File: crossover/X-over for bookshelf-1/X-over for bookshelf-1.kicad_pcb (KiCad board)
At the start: 2 copper layers, 10 parts, among them J1 Screw_Terminal_01x02, J2 Screw_Terminal_01x04

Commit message: adding KiCAD documents for the XO design
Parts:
- moved C2 96.0 mm to (134.1, 132.1), turned to 180 degrees
- moved J2 64.5 mm to (193.0, 113.3), turned to 90 degrees
- moved L1 33.1 mm to (185.4, 49.0)
- moved J1 16.5 mm to (182.4, 38.1)
- moved C3 13.7 mm to (120.3, 68.6)
- moved C1 10.5 mm to (120.3, 45.7)
- moved R1 10.2 mm to (134.6, 104.1)
- moved R2 10.2 mm to (73.7, 86.4)
- moved L3 9.16 mm to (179.2, 106.7)
- moved L2 5.68 mm to (80.9, 55.9)
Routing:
- net Net-(J2-Pin_4): track 140.7 -> 31.9 mm
- net Net-(C2-Pad2): track 50.2 -> 115.6 mm
- net Net-(J2-Pin_2): track 156.3 -> 185.5 mm
- net Net-(J2-Pin_1): track 122.7 -> 146.5 mm
- net Net-(J1-Pin_2): track 157.1 -> 139.0 mm
- net Net-(J1-Pin_1): track 46.5 -> 32.1 mm
- net Net-(C3-Pad1): track 37.8 -> 23.7 mm
- net Net-(L3-Pad2): track 16.4 -> 12.4 mm
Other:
- board outline added: 139.7 x 119.4 mm

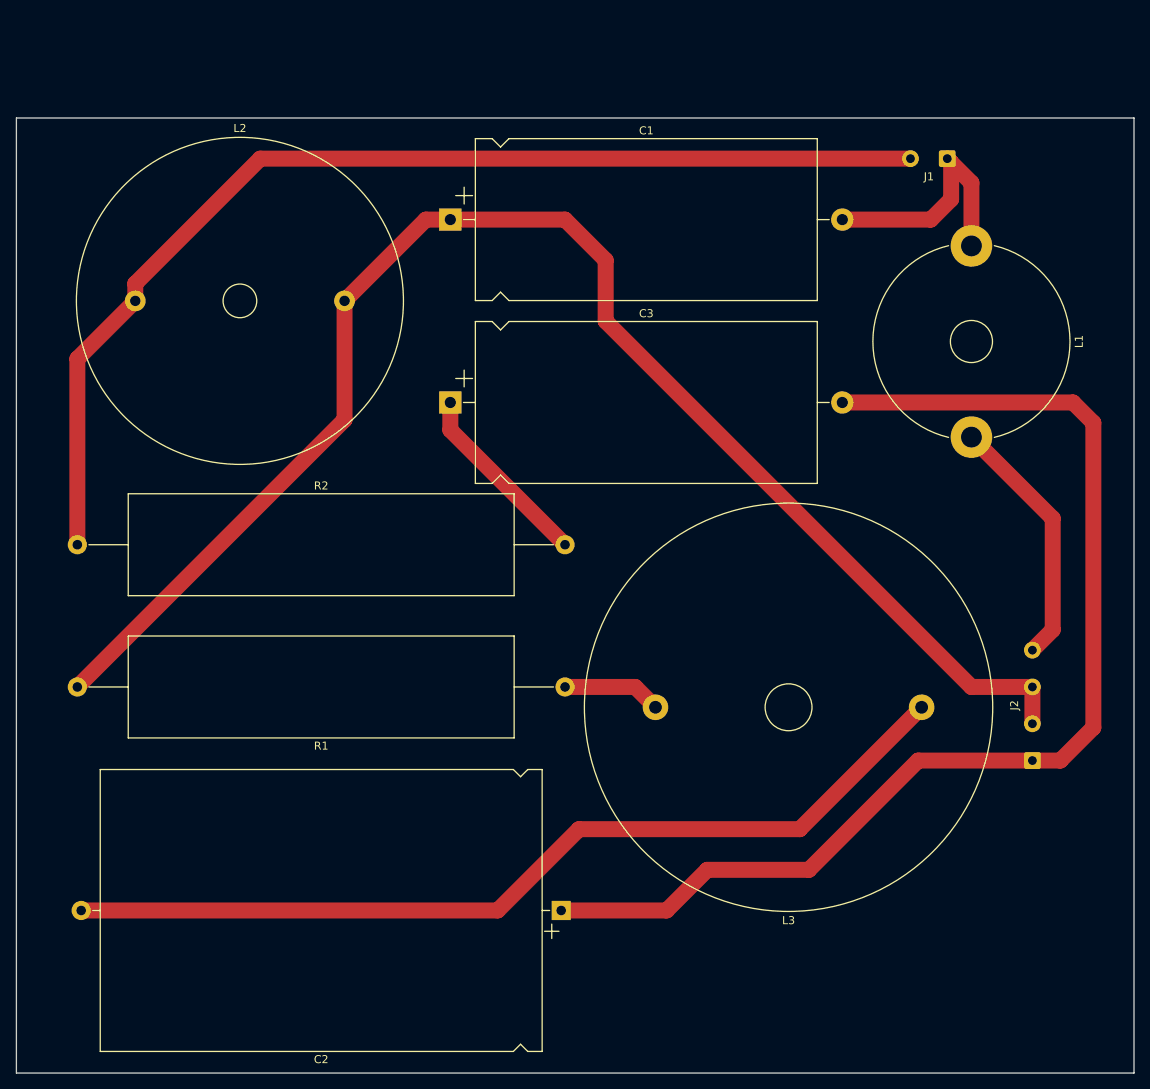
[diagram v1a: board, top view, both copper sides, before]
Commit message: Feature/pcb updates (#3)
* adding intial work to support PCB draw

* Minimizing overall PCB size

Now it should both fit inside the cabinet as well as through the driver opening.
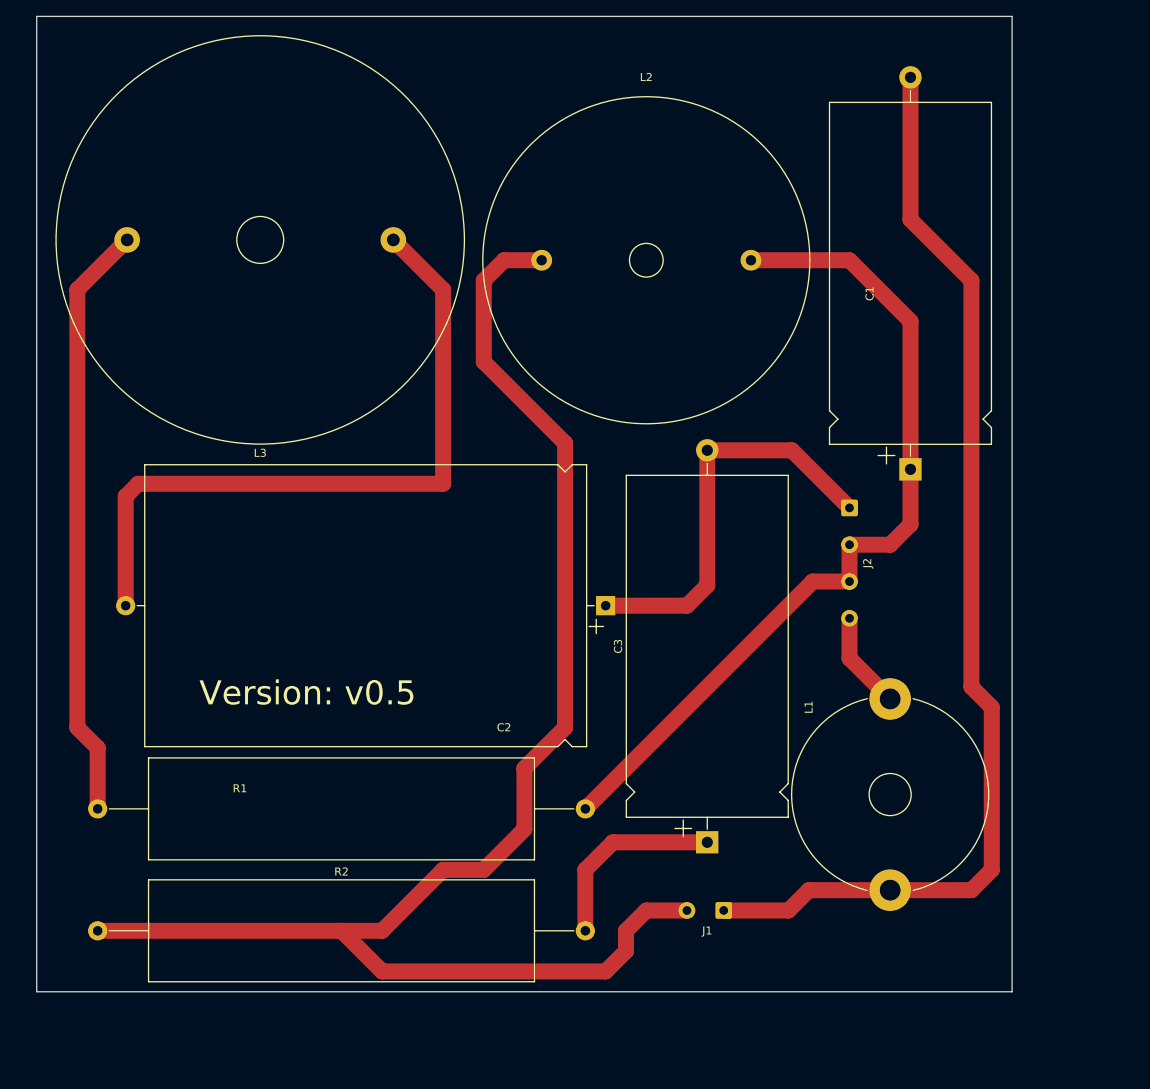
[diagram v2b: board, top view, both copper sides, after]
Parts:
- moved J1 98.0 mm to (154.5, 132.1)
- moved L3 88.2 mm to (113.2, 48.3)
- moved L1 81.2 mm to (175.3, 129.5), turned to 90 degrees
- moved C1 65.4 mm to (177.8, 76.9), turned to 90 degrees
- moved C3 63.7 mm to (152.4, 123.6), turned to 90 degrees
- moved R1 60.4 mm to (76.2, 119.4), turned to 0 degrees
- moved L2 51.1 mm to (131.7, 50.8)
- moved R2 48.3 mm to (76.2, 134.6)
- moved J2 39.0 mm to (170.2, 81.8), turned to -90 degrees
- moved C2 38.5 mm to (139.7, 94.0)
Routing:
- net Net-(J1-Pin_1): track 32.1 -> 138.9 mm
- net Net-(J2-Pin_1): track 146.5 -> 51.4 mm
- net Net-(J2-Pin_2): track 185.5 -> 106.6 mm
- net Net-(L3-Pad2): track 12.4 -> 74.8 mm
- net Net-(J1-Pin_2): track 139.0 -> 191.7 mm
- net Net-(C2-Pad2): track 115.6 -> 87.1 mm
- net Net-(J2-Pin_4): track 31.9 -> 12.2 mm
- net Net-(C3-Pad1): track 23.7 -> 24.3 mm
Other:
- board size 139.7 x 119.4 mm -> 121.9 x 121.9 mm
- board text added: "Version: v0.5"

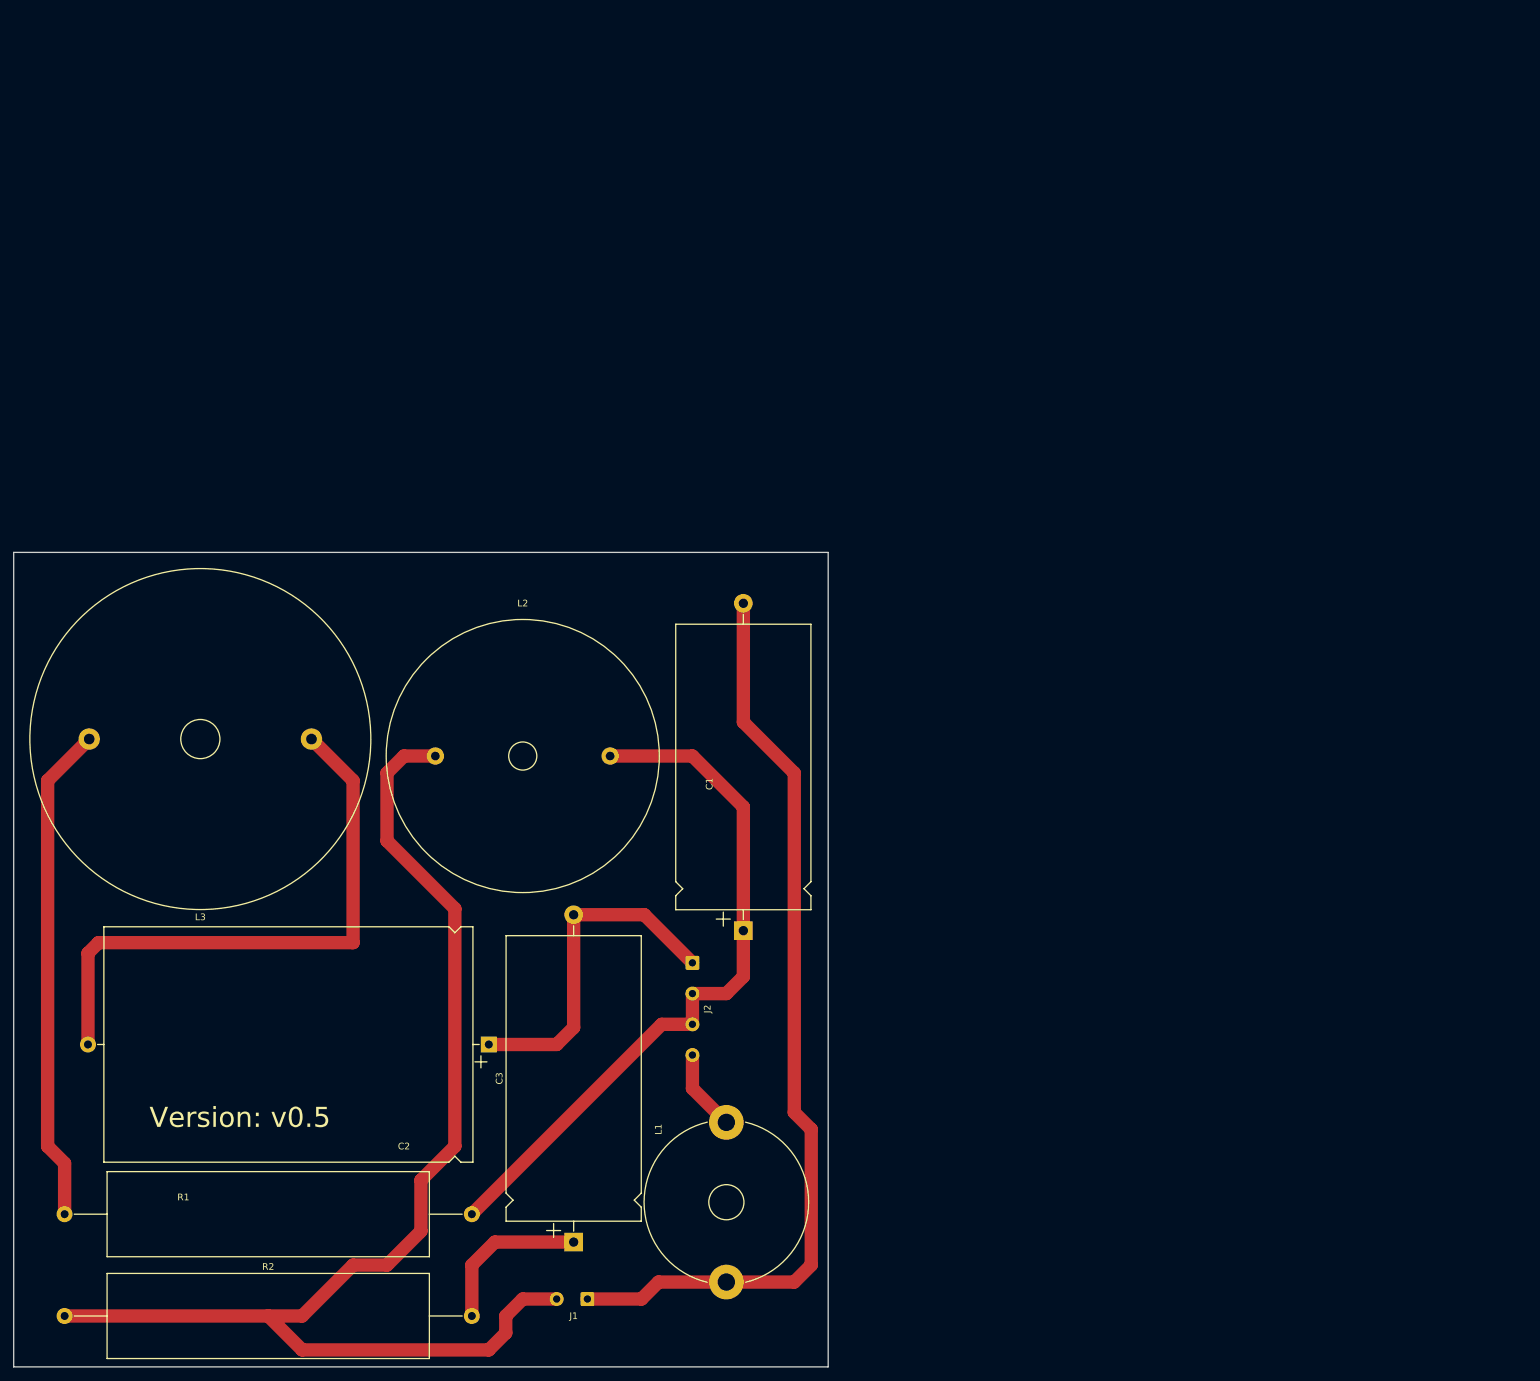
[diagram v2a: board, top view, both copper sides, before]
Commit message: Updated schematic and board layout, according to PdB Spec (#4)
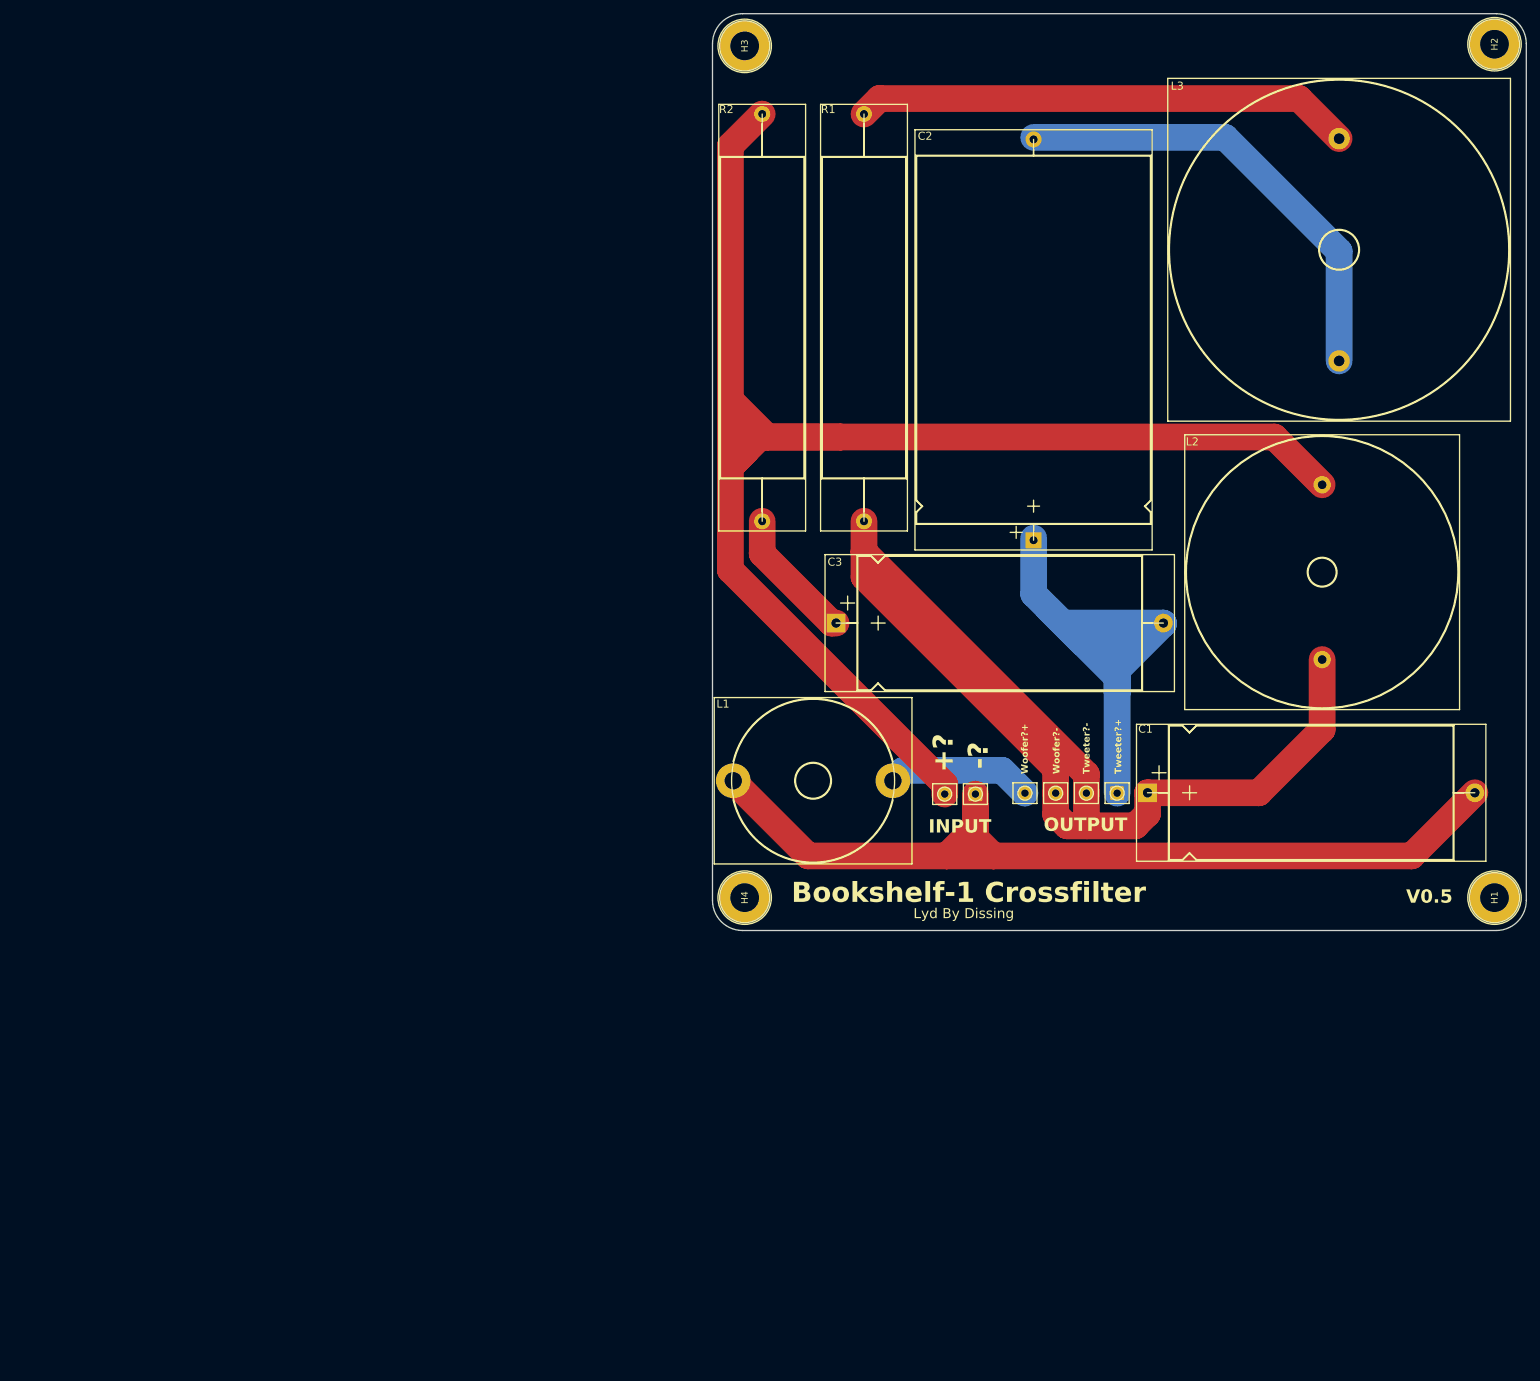
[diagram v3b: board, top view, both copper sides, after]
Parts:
- added H1: MountingHole, MountingHole:MountingHole_4.3mm_M4_DIN965_Pad, F.Cu at (290.2, 72.0)
- added H2: MountingHole, MountingHole:MountingHole_4.3mm_M4_DIN965_Pad, F.Cu at (290.2, -55.8)
- added H3: MountingHole, MountingHole:MountingHole_4.3mm_M4_DIN965_Pad, F.Cu at (178.0, -55.5)
- added H4: MountingHole, MountingHole:MountingHole_4.3mm_M4_DIN965_Pad, F.Cu at (178.0, 72.0)
- J1: value Screw_Terminal_01x02 -> Input
- J2: value Screw_Terminal_01x04 -> Output
- L3: value 0,1mH -> 0.1mH
- R1: value 1,8Ω -> 1.8Ω
- moved R2 208.0 mm to (180.6, -45.3), turned to -90 degrees
- moved R1 203.6 mm to (195.9, -45.3), turned to -90 degrees
- moved L3 163.9 mm to (267.0, -8.35), turned to 90 degrees
- moved L2 138.8 mm to (264.4, 10.2), turned to -90 degrees
- moved C2 111.1 mm to (221.2, 18.5), turned to 90 degrees
- moved C3 100.6 mm to (191.7, 30.9), turned to 0 degrees
- moved J1 95.3 mm to (212.5, 56.5)
- moved L1 75.0 mm to (176.3, 54.5), turned to 0 degrees
- moved J2 68.5 mm to (233.8, 56.4), turned to 180 degrees
- moved C1 63.9 mm to (238.3, 56.3), turned to 0 degrees
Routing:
- net Net-(J2-Pin_2): track 106.6 -> 169.5 mm
- net Net-(J1-Pin_2): track 191.7 -> 235.3 mm
- net Net-(J2-Pin_1): track 51.4 -> 86.1 mm
- net Net-(C2-Pad2): track 87.1 -> 69.2 mm
- net Net-(J2-Pin_4): track 12.2 -> 21.8 mm
- net Net-(C3-Pad1): track 24.3 -> 20.2 mm
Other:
- board size 121.9 x 121.9 mm -> 121.8 x 137.2 mm
- board text added: "+?"
- board text added: "-?"
- board text added: "Bookshelf-1 Crossfilter"
- board text added: "INPUT"
- board text added: "Lyd By Dissing"
- board text added: "OUTPUT"
- board text added: "Tweeter?+"
- board text added: "Tweeter?-"
- board text added: "V0.5"
- board text added: "Woofer?+"
- board text added: "Woofer?-"
- board text removed: "Version: v0.5"

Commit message: changing font to roboto
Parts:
- moved C1 165.7 mm to (108.5, 159.2)
- moved C2 165.7 mm to (91.4, 121.4)
- moved C3 165.7 mm to (61.9, 133.8)
- moved H1 165.7 mm to (160.4, 174.9)
- moved H2 165.7 mm to (160.4, 47.2)
- moved H3 165.7 mm to (48.2, 47.4)
- moved H4 165.7 mm to (48.2, 174.9)
- moved J2 165.7 mm to (104.0, 159.3)
- moved L2 165.7 mm to (134.6, 113.1)
- moved L3 165.7 mm to (137.2, 94.6)
- moved R1 165.7 mm to (66.1, 57.6)
- moved R2 165.7 mm to (50.8, 57.6)
- moved J1 165.7 mm to (82.7, 159.4)
- moved L1 165.7 mm to (46.5, 157.4)
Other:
- board text added: "+"
- board text added: "-"
- board text added: "Bookshelf-1 Crossover"
- board text added: "Tweeter+"
- board text added: "Tweeter-"
- board text added: "Woofer+"
- board text added: "Woofer-"
- board text removed: "+?"
- board text removed: "-?"
- board text removed: "Bookshelf-1 Crossfilter"
- board text removed: "Tweeter?+"
- board text removed: "Tweeter?-"
- board text removed: "Woofer?+"
- board text removed: "Woofer?-"

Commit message: adding logo as graphic
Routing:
- net Net-(J2-Pin_2): track 169.5 -> 176.6 mm
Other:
- board text added: "v0.6"
- board text removed: "V0.5"
